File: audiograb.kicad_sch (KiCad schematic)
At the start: 8 parts, among them J2 USB_C_Receptacle_USB2.0_16P

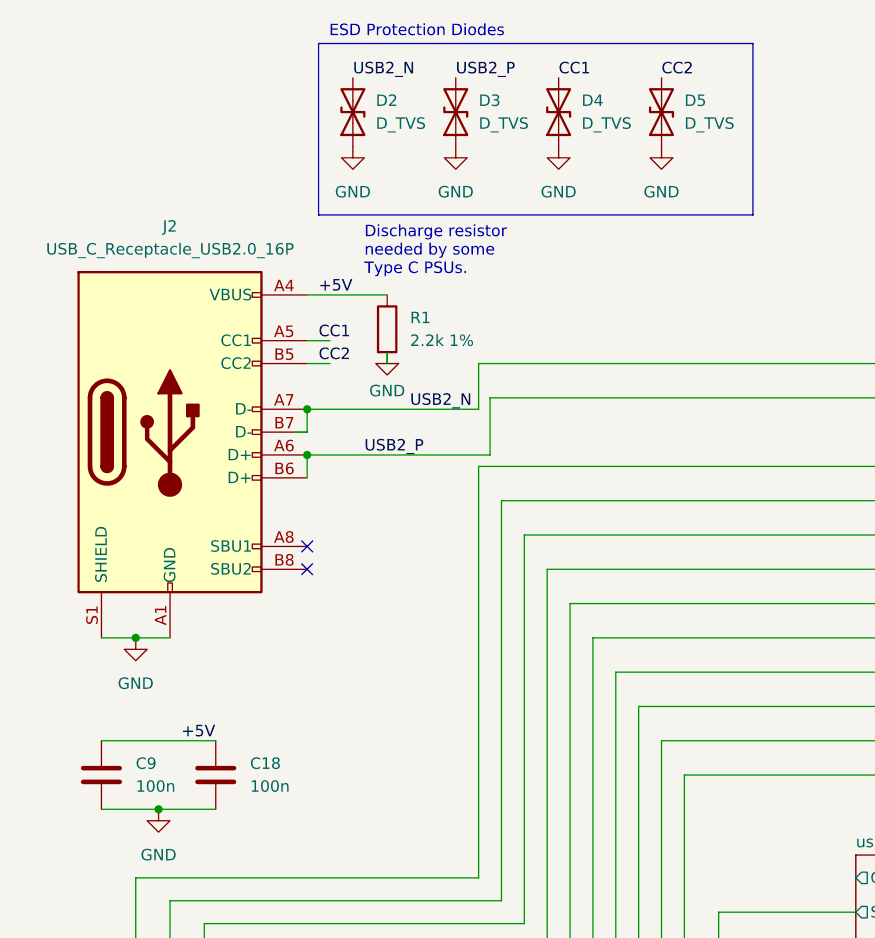
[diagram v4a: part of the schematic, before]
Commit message: added cap footprints and part numbers
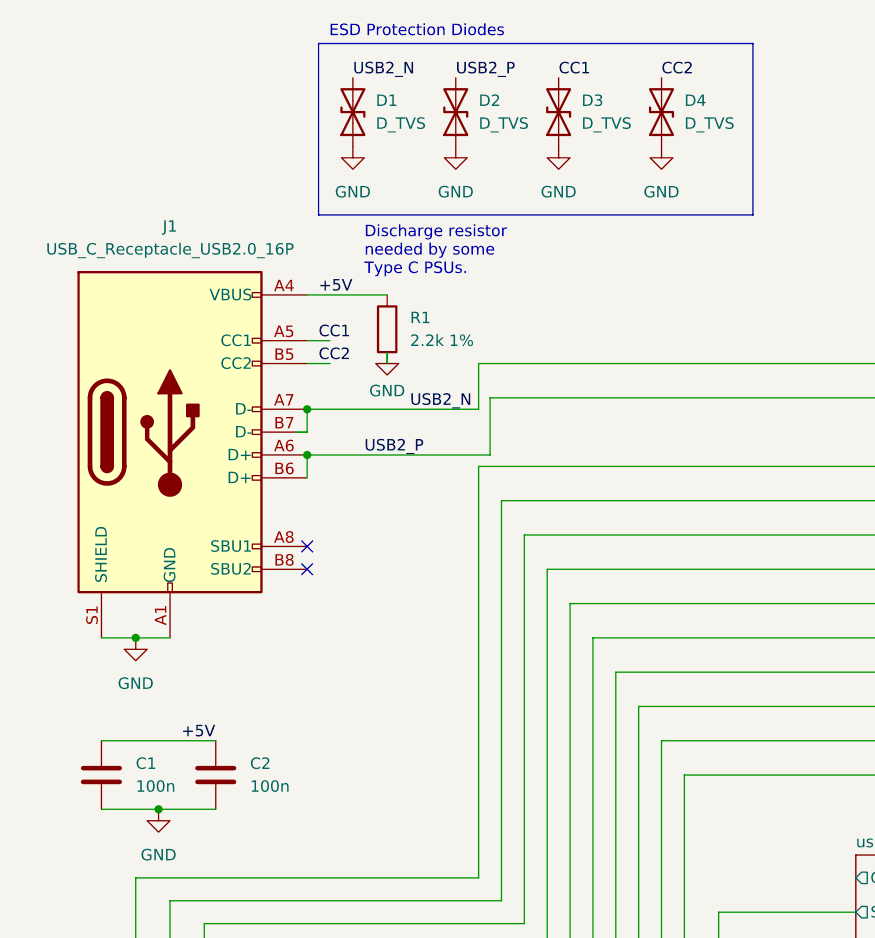
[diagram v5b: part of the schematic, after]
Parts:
- C1: renamed from C9; footprint (none) -> Capacitor_SMD:C_0603_1608Metric; MPN (none) -> C0603C104K3RACTU
- C2: renamed from C18; footprint (none) -> Capacitor_SMD:C_0603_1608Metric; MPN (none) -> C0603C104K3RACTU
- renumbered D2 to D1, D3 to D2, D4 to D3, D5 to D4, J2 to J1
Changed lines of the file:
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@@
 		(dnp no)
 		(fields_autoplaced yes)
-		(property "Reference" "#PWR04"
+		(property "Reference" "#PWR02"
 			(at 35.56 107.95 0)
 			(effects
@@
 			(project ""
 				(path "/c46c2311-6d4b-411d-b012-c7730eac136d"
-					(reference "#PWR04")
+					(reference "#PWR02")
 					(unit 1)
 				)
@@
 		(dnp no)
 		(fields_autoplaced yes)
-		(property "Reference" "D2"
+		(property "Reference" "D1"
 			(at 59.69 22.8599 90)
 			(effects
@@
 			(project ""
 				(path "/c46c2311-6d4b-411d-b012-c7730eac136d"
-					(reference "D2")
+					(reference "D1")
 					(unit 1)
 				)
@@
 		(on_board yes)
 		(dnp no)
-		(property "Reference" "#PWR02"
+		(property "Reference" "#PWR04"
 			(at 60.96 57.15 0)
 			(effects
@@
 			(project ""
 				(path "/c46c2311-6d4b-411d-b012-c7730eac136d"
-					(reference "#PWR02")
+					(reference "#PWR04")
 					(unit 1)
 				)
@@
 		(on_board yes)
 		(dnp no)
-		(property "Reference" "C9"
+		(property "Reference" "C1"
 			(at 33.02 96.5199 0)
 			(effects
@@
 			)
 		)
-		(property "Footprint" ""
+		(property "Footprint" "Capacitor_SMD:C_0603_1608Metric"
 			(at 30.1752 101.6 0)
 			(effects
@@
 			)
 		)
+		(property "MPN" "C0603C104K3RACTU"
+			(at 29.21 97.79 0)
+			(effects
+				(font
+					(size 1.27 1.27)
+				)
+				(hide yes)
+			)
+		)
 		(pin "2"
 		)
@@
 			(project ""
 				(path "/c46c2311-6d4b-411d-b012-c7730eac136d"
-					(reference "C9")
+					(reference "C1")
 					(unit 1)
 				)
@@
 		(dnp no)
 		(fields_autoplaced yes)
-		(property "Reference" "J2"
+		(property "Reference" "J1"
 			(at 36.83 36.83 0)
 			(effects
@@
 			(project ""
 				(path "/c46c2311-6d4b-411d-b012-c7730eac136d"
-					(reference "J2")
+					(reference "J1")
 					(unit 1)
 				)
@@
 		(dnp no)
 		(fields_autoplaced yes)
-		(property "Reference" "D4"
+		(property "Reference" "D3"
 			(at 82.55 22.8599 90)
 			(effects
@@
 			(project "audiograb"
 				(path "/c46c2311-6d4b-411d-b012-c7730eac136d"
-					(reference "D4")
+					(reference "D3")
 					(unit 1)
 				)
@@
 		(dnp no)
 		(fields_autoplaced yes)
-		(property "Reference" "D5"
+		(property "Reference" "D4"
 			(at 93.98 22.8599 90)
 			(effects
@@
 			(project "audiograb"
 				(path "/c46c2311-6d4b-411d-b012-c7730eac136d"
-					(reference "D5")
+					(reference "D4")
 					(unit 1)
 				)
@@
 		(dnp no)
 		(fields_autoplaced yes)
-		(property "Reference" "#PWR05"
+		(property "Reference" "#PWR03"
 			(at 57.15 34.29 0)
 			(effects
@@
 			(project ""
 				(path "/c46c2311-6d4b-411d-b012-c7730eac136d"
-					(reference "#PWR05")
+					(reference "#PWR03")
 					(unit 1)
 				)
@@
 		(dnp no)
 		(fields_autoplaced yes)
-		(property "Reference" "#PWR01"
+		(property "Reference" "#PWR05"
 			(at 68.58 34.29 0)
 			(effects
@@
 			(project ""
 				(path "/c46c2311-6d4b-411d-b012-c7730eac136d"
-					(reference "#PWR01")
+					(reference "#PWR05")
 					(unit 1)
 				)
@@
 		(dnp no)
 		(fields_autoplaced yes)
-		(property "Reference" "D3"
+		(property "Reference" "D2"
 			(at 71.12 22.8599 90)
 			(effects
@@
 			(project "audiograb"
 				(path "/c46c2311-6d4b-411d-b012-c7730eac136d"
-					(reference "D3")
+					(reference "D2")
 					(unit 1)
 				)
@@
 		(dnp no)
 		(fields_autoplaced yes)
-		(property "Reference" "C18"
+		(property "Reference" "C2"
 			(at 45.72 96.5199 0)
 			(effects
@@
 			)
 		)
-		(property "Footprint" ""
+		(property "Footprint" "Capacitor_SMD:C_0603_1608Metric"
 			(at 42.8752 101.6 0)
 			(effects
@@
 			)
 		)
+		(property "MPN" "C0603C104K3RACTU"
+			(at 41.91 97.79 0)
+			(effects
+				(font
+					(size 1.27 1.27)
+				)
+				(hide yes)
+			)
+		)
 		(pin "2"
 		)
@@
 			(project "audiograb"
 				(path "/c46c2311-6d4b-411d-b012-c7730eac136d"
-					(reference "C18")
+					(reference "C2")
 					(unit 1)
 				)
@@
 		(dnp no)
 		(fields_autoplaced yes)
-		(property "Reference" "#PWR03"
+		(property "Reference" "#PWR01"
 			(at 33.02 88.9 0)
 			(effects
@@
 			(project ""
 				(path "/c46c2311-6d4b-411d-b012-c7730eac136d"
-					(reference "#PWR03")
-					(unit 1)
-				)
+					(reference "#PWR01")
+					(unit 1)
+				)

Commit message: added footprints fore resistors
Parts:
- R1: footprint (none) -> Resistor_SMD:R_0603_1608Metric; MPN (none) -> RC0603FR-072K2L
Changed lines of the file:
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@@
 			)
 		)
-		(property "Footprint" ""
+		(property "Footprint" "Resistor_SMD:R_0603_1608Metric"
 			(at 59.182 48.26 90)
 			(effects
@@
 			(at 60.96 48.26 0)
 			(effects
+				(font
+					(size 1.27 1.27)
+				)
+				(hide yes)
+			)
+		)
+		(property "MPN" "RC0603FR-072K2L"
+			(at 60.96 48.26 0)
+			(effects

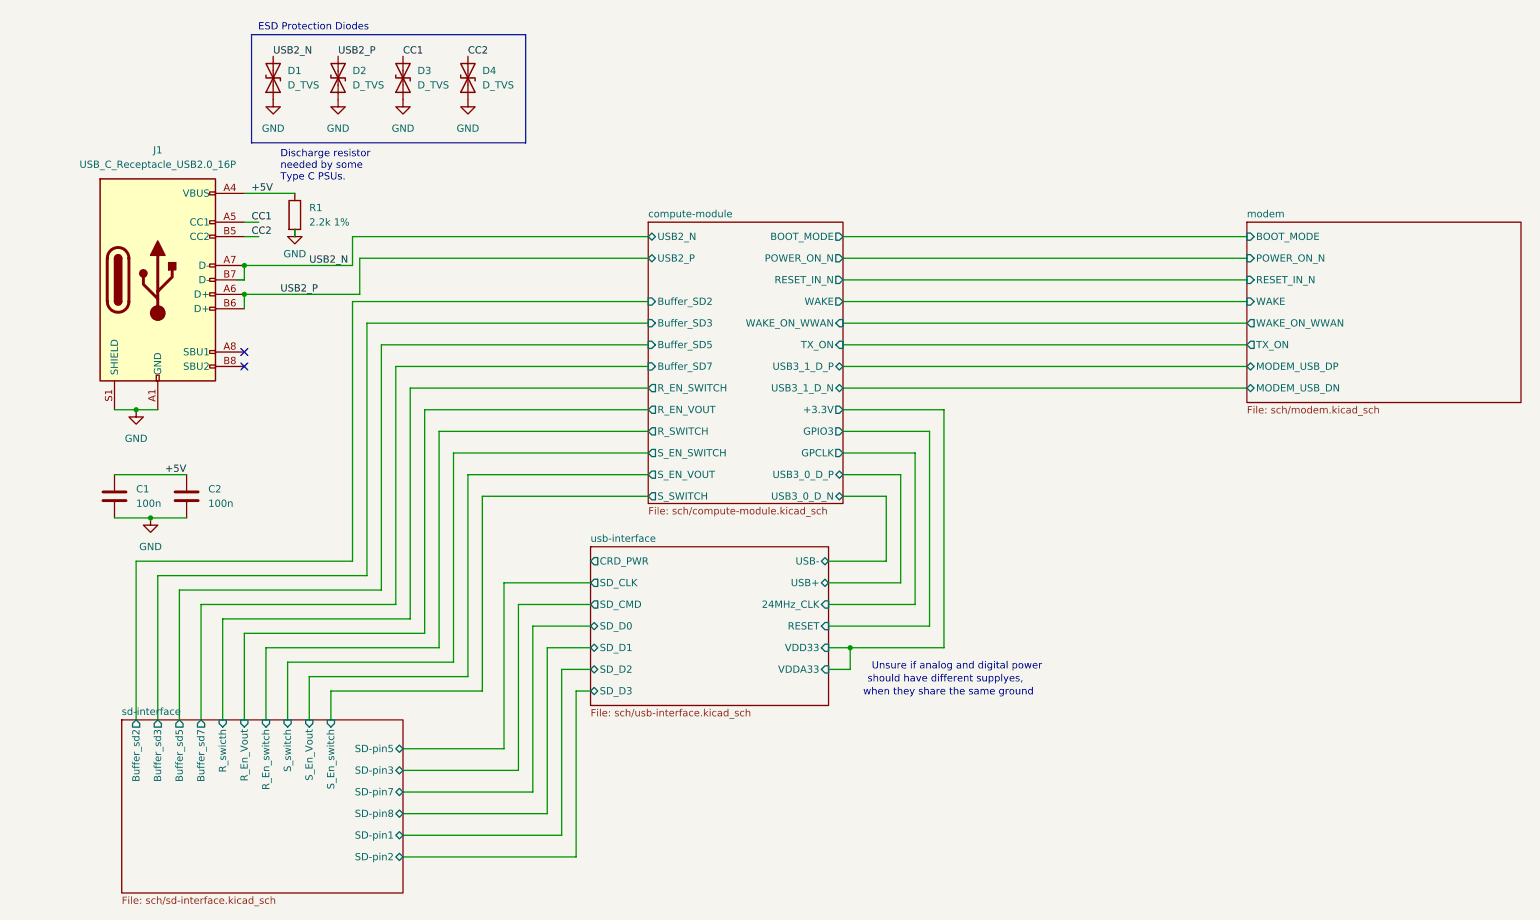
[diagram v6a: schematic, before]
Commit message: added more footprinst and esd
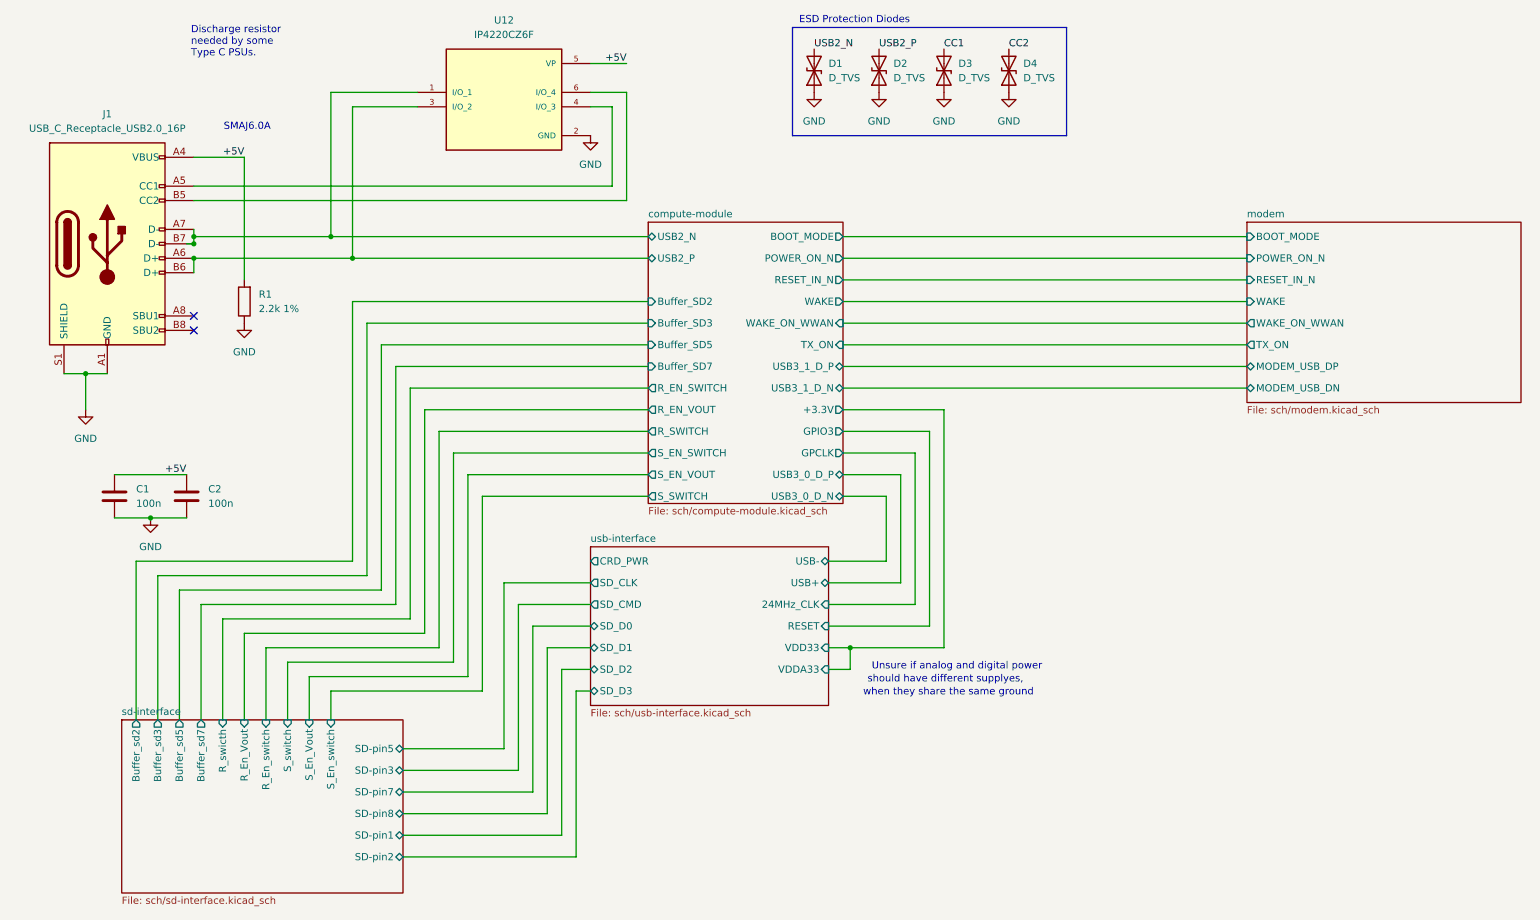
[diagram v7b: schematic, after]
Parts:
- added U12: IP4220CZ6F, IP4220CZ6F:SOT95P275X110-6N, symbol IP4220CZ6F:IP4220CZ6F
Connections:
- net +5V: now also R1.2, U12.5 (VP); no longer R1.1
- net CC1: no longer J1.A5 (CC1)
- net CC2: no longer J1.B5 (CC2)
- net GND: now also R1.1, U12.2 (GND); no longer R1.2
- net USB2_N: no longer J1.A7 (D-), J1.B7 (D-)
- net USB2_P: no longer J1.A6 (D+), J1.B6 (D+)
- new net: J1.A5 (CC1), U12.4 (I/O_3)
- new net: J1.B5 (CC2), U12.6 (I/O_4)
- new net compute-module/USB2_N: J1.A7 (D-), J1.B7 (D-), U12.1 (I/O_1)
- new net compute-module/USB2_P: J1.A6 (D+), J1.B6 (D+), U12.3 (I/O_2)
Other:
- note added: "SMAJ6.0A"
- moved on the sheet: D1, D2, D3, D4, J1, R1

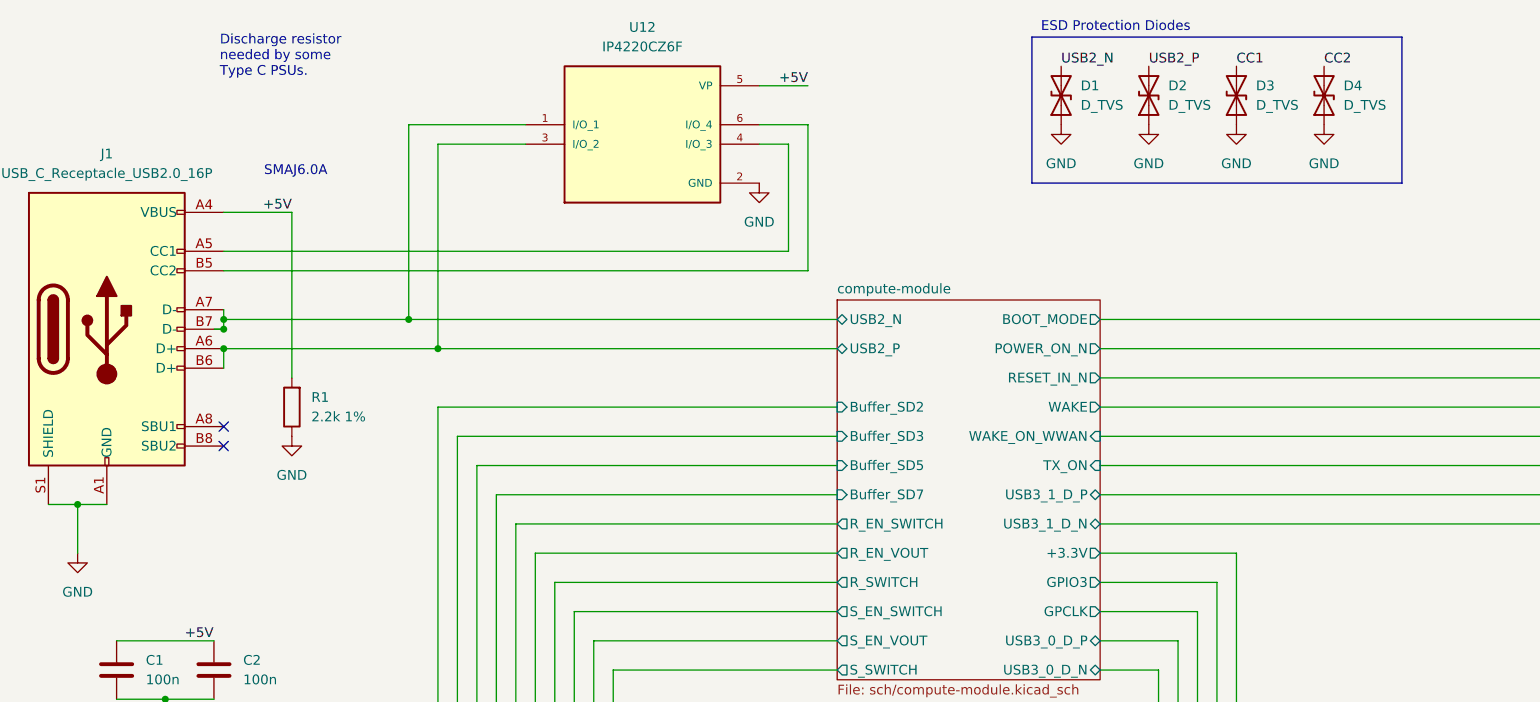
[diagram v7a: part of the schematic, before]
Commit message: added more footprints and added to pcb
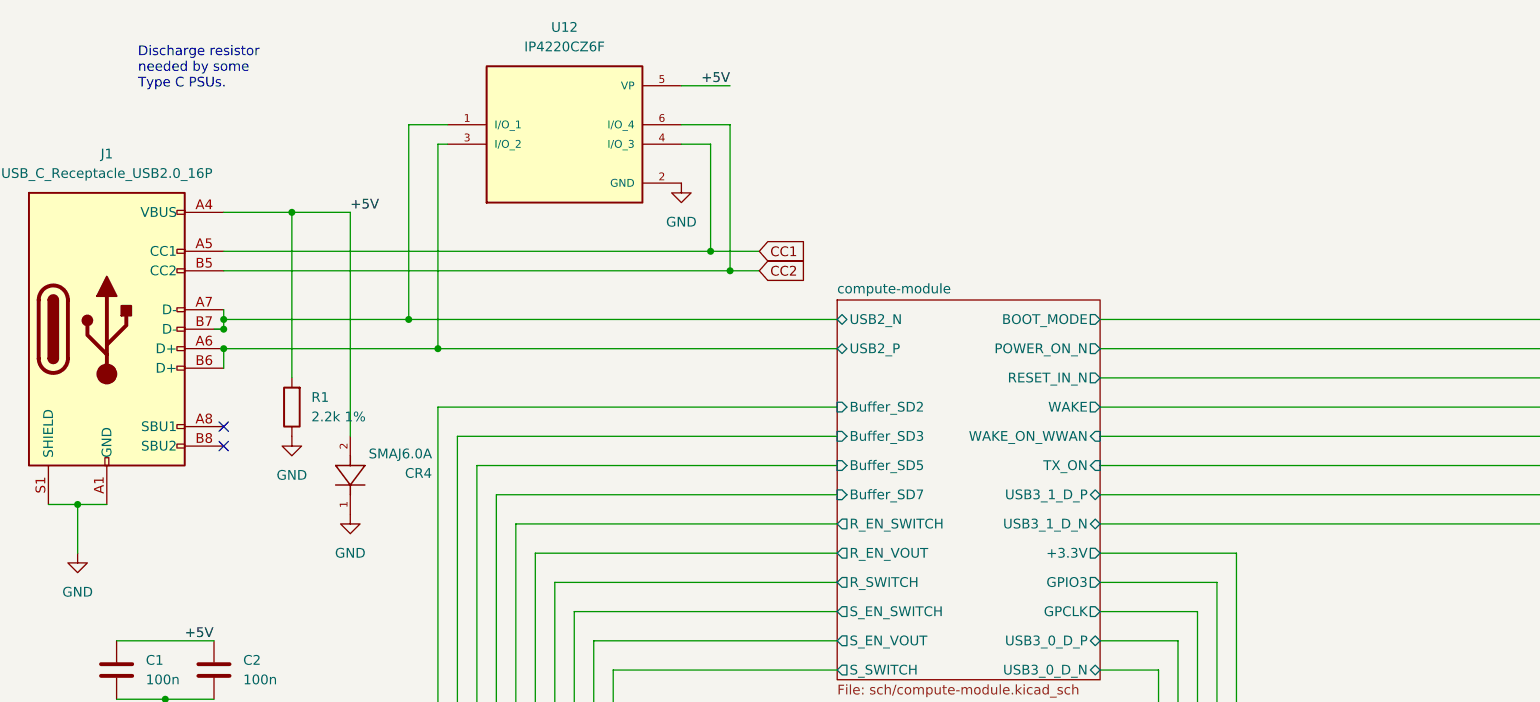
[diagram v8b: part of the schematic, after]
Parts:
- removed D1, D2, D3, D4: D_TVS, symbol Device:D_TVS
- added CR4: SMAJ6.0A, SMAJ6.0A:SMASERIES_LTF, symbol SMAJ6.0A:SMAJ6.0A
- J1: footprint (none) -> Connector_USB:USB_C_Receptacle_GCT_USB4105-xx-A_16P_TopMnt_Horizontal
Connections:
- net +5V: now also CR4.2
- net CC1: now also J1.A5 (CC1), U12.4 (I/O_3)
- net CC2: now also J1.B5 (CC2), U12.6 (I/O_4)
- net GND: now also CR4.1
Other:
- note removed: "ESD Protection Diodes"
- note removed: "SMAJ6.0A"
- moved on the sheet: U12
